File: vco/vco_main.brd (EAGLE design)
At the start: 94.9 x 107.9 mm, 101 parts, among them IC1 OPA4130U, IC2 LM13700M, IC3 OPA4130U, IC4 OPA4130U, Q1 MMBFJ3

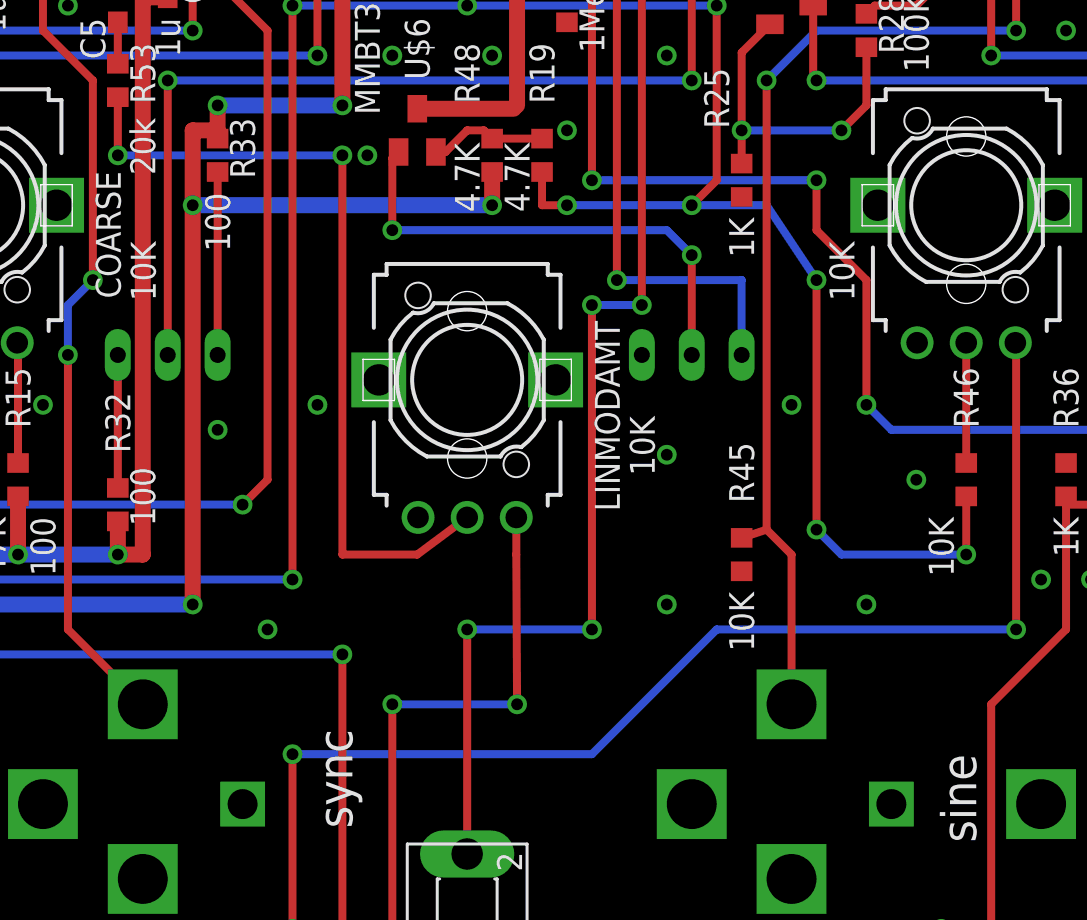
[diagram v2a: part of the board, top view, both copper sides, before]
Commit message: added 2 board rev of the vcf in a separate folder
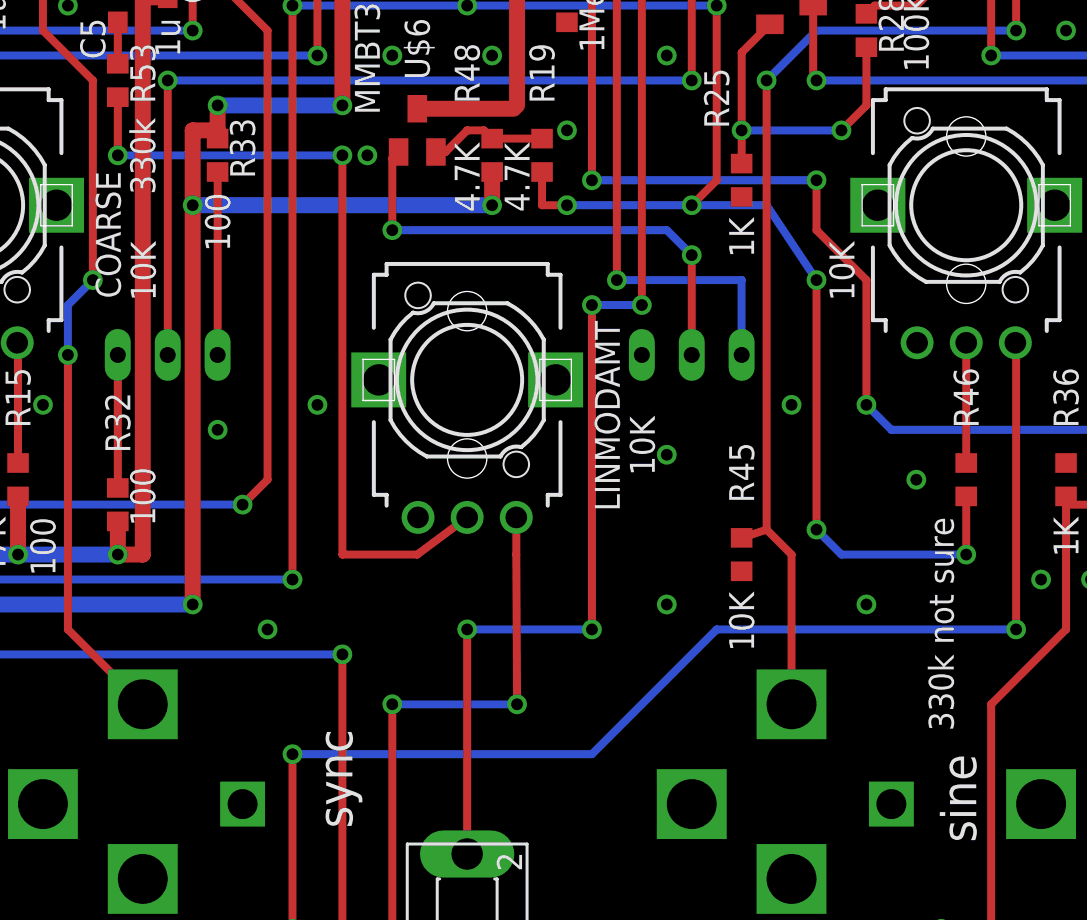
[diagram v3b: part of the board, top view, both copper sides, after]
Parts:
- R46: value 10K -> 330k not sure
- R53: value 20k -> 330k
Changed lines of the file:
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@@
 <attribute name="VALUE" x="61.595" y="34.925" size="1.27" layer="21" font="vector" ratio="15" rot="R270"/>
 </element>
-<element name="R46" library="dan" package="R0603" value="10K" x="73.66" y="40.64" smashed="yes" rot="R90">
+<element name="R46" library="dan" package="R0603" value="330k not sure" x="73.66" y="40.64" smashed="yes" rot="R90">
 <attribute name="NAME" x="73.025" y="46.355" size="1.27" layer="21" font="vector" ratio="15" rot="R270"/>
 <attribute name="VALUE" x="71.755" y="38.735" size="1.27" layer="21" font="vector" ratio="15" rot="R270"/>
@@
 <attribute name="VALUE" x="3.175" y="19.685" size="1.27" layer="21" font="vector" ratio="15" rot="R270"/>
 </element>
-<element name="R53" library="dan" package="R0603" value="20k" x="30.48" y="60.96" smashed="yes" rot="R90">
+<element name="R53" library="dan" package="R0603" value="330k" x="30.48" y="60.96" smashed="yes" rot="R90">
 <attribute name="NAME" x="31.115" y="62.865" size="1.27" layer="21" font="vector" ratio="15" rot="R270"/>
 <attribute name="VALUE" x="31.115" y="59.055" size="1.27" layer="21" font="vector" ratio="15" rot="R270"/>
